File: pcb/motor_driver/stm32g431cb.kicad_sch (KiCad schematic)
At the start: 52 parts, among them J3 Conn_ARM_JTAG_SWD_10, J4 UART1 SH, J5 Conn, Q1 BSS138, SW1 SKRPACE010, SW2 SKRPACE010, U10 STM32G431CB, U11 USBLC6-4SC6, U12 MCP2562-E-SN, U13 USBLC6-4SC6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

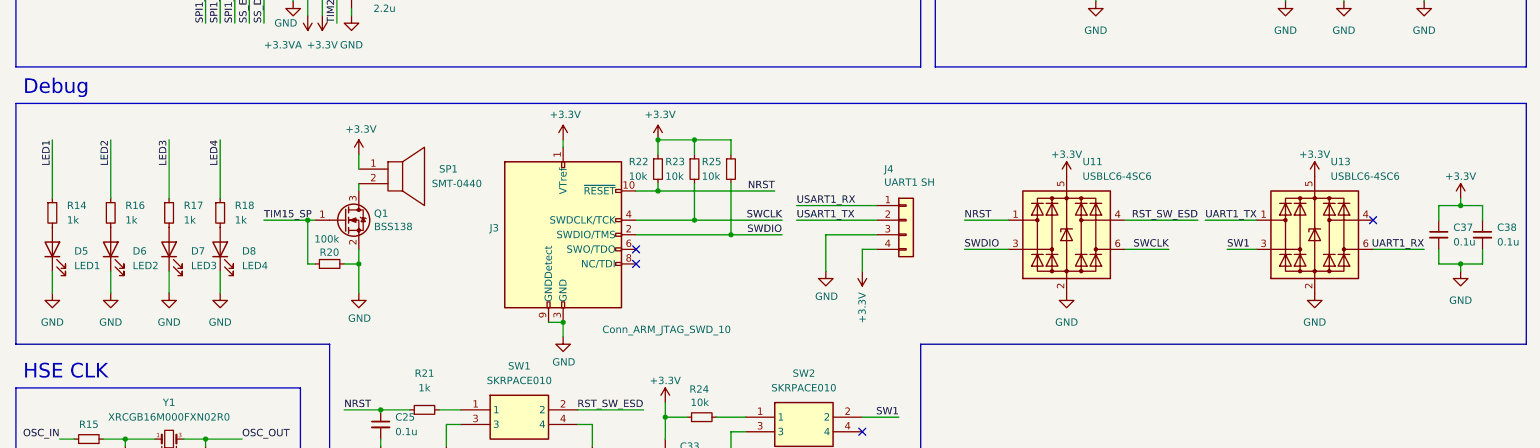
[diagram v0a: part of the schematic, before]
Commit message: delete ESD protection
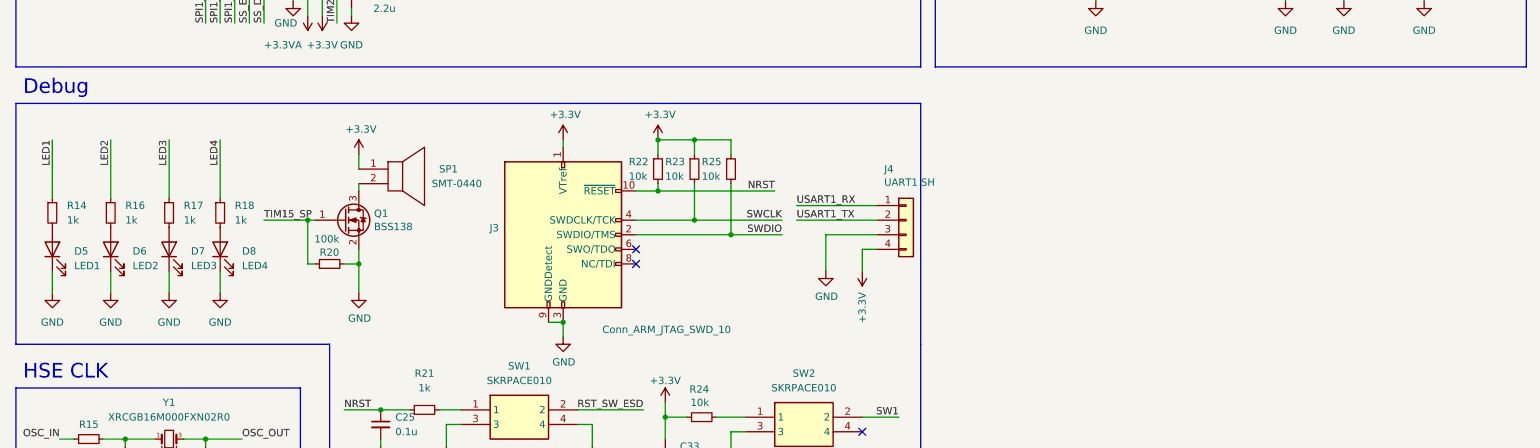
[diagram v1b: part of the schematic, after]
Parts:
- removed C37, C38: 0.1u, Capacitor_SMD:C_0603_1608Metric_Pad1.08x0.95mm_HandSolder, symbol Device:C_Small
- removed U11, U13: USBLC6-4SC6, Package_TO_SOT_SMD:SOT-23-6, symbol Power_Protection:USBLC6-4SC6
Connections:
- no-connect marks 4 -> 3

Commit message: update pcb
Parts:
- removed C31, C32: 0.1u, Capacitor_SMD:C_0201_0603Metric, symbol Device:C_Small
- removed C35: 1u, Capacitor_SMD:C_0201_0603Metric, symbol Device:C_Small
- C34: value 0.01u -> 0.1u
- C36: footprint Capacitor_SMD:C_0603_1608Metric_Pad1.08x0.95mm_HandSolder -> Capacitor_SMD:C_0201_0603Metric
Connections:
- net SPI1_SCK is gone; now on net SPI1_CLK: U10.13 (PA5)
- net CAN_H: now also J5.3 (Pin_3); no longer J5.2 (Pin_2)
- net CAN_L: now also J5.2 (Pin_2); no longer J5.3 (Pin_3)
- net DRV_CAL: now also U10.11 (PA3); no longer U10.4 (PC15)
- net DRV_ENABLE: now also U10.2 (PC13); no longer U10.3 (PC14)
- net FAULTB: now also U10.3 (PC14); no longer U10.2 (PC13)
- net HALL_U: now also U10.40 (PB3); no longer U10.43 (PB6)
- net HALL_V: now also U10.41 (PB4); no longer U10.42 (PB5)
- net HALL_W: now also U10.39 (PA15); no longer U10.41 (PB4)
- net INHA: now also U10.43 (PB6); no longer U10.39 (PA15)
- net INHB: now also U10.44 (PB7); no longer U10.40 (PB3)
- net INHC: now also U10.46 (PB9); no longer U10.22 (PB10)
- net INLX: now also U10.12 (PA4); no longer U10.30 (PA8)
- net LED1: now also U10.17 (PB1); no longer U10.11 (PA3)
- net LED2: now also U10.18 (PB2); no longer U10.12 (PA4)
- net LED3: now also U10.22 (PB10); no longer U10.46 (PB9)
- net LED4: now also U10.25 (PB11); no longer U10.44 (PB7)
- net LED_CAN_RX: now also U10.29 (PB15); no longer U10.27 (PB13)
- net LED_CAN_TX: now also U10.30 (PA8); no longer U10.26 (PB12)
- net SOA: now also U10.10 (PA2); no longer U10.8 (PA0)
- net SOC: now also U10.8 (PA0); no longer U10.10 (PA2)
- net SS_DRV: now also U10.4 (PC15); no longer U10.17 (PB1)
- net SS_ENC: now also U10.42 (PB5); no longer U10.16 (PB0)
- net SW1: now also U10.16 (PB0); no longer U10.25 (PB11)
- net RST_SW_ESD: no longer names the net of SW1.2
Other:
- note added: "VDD"
- note added: "VDDA"
- note added: "Vref"
- moved on the sheet: C36

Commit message: feat: fix most bug
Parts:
- removed J4: UART1 SH, Connector_PinHeader_2.54mm:PinHeader_1x04_P2.54mm_Vertical, symbol Connector_Generic:Conn_01x04
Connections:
- net DRV_ENABLE: now also U10.4 (PC15); no longer U10.2 (PC13)
- net FAULTB: now also U10.2 (PC13); no longer U10.3 (PC14)
- net HALL_V: now also U10.39 (PA15); no longer U10.41 (PB4)
- net HALL_W: now also U10.41 (PB4); no longer U10.39 (PA15)
- net LED_CAN_RX: now also U10.26 (PB12); no longer U10.29 (PB15)
- net SS_DRV: now also U10.3 (PC14); no longer U10.4 (PC15)
- net SPI2_CLK: now reaches U10.27 (PB13)
- net USART1_RX renamed SPI2_MISO
- net USART1_TX: no longer names the net of U10.31 (PA9)
- new net SPI2_MOSI: U10.29 (PB15)

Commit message: chore: commit before starting to develop v1.2
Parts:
- removed C22, C23, C24, C28: 2.2u, Capacitor_SMD:C_0402_1005Metric, symbol Device:C_Small
- removed Q1: BSS138, Package_TO_SOT_SMD:SOT-23, symbol Transistor_FET:BSS138
- removed R20: 100k, Resistor_SMD:R_0201_0603Metric, symbol Device:R_Small
- removed R21: 1k, Resistor_SMD:R_0603_1608Metric_Pad0.98x0.95mm_HandSolder, symbol Device:R_Small
- removed SP1: SMT-0440, omni:STM0440-T-R, symbol My_Device:SMT-0440
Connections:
- net GND: now also U10.19 (VSSA), U10.23 (VSS), U10.35 (VSS), U10.47 (VSS)
- net NRST: now also SW1.1
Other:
- moved on the sheet: C25
